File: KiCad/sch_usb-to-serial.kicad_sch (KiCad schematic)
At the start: 14 parts, among them J2 ESPFlash, Q1 MMDT3904, U3 CP2102N-Axx-xQFN24

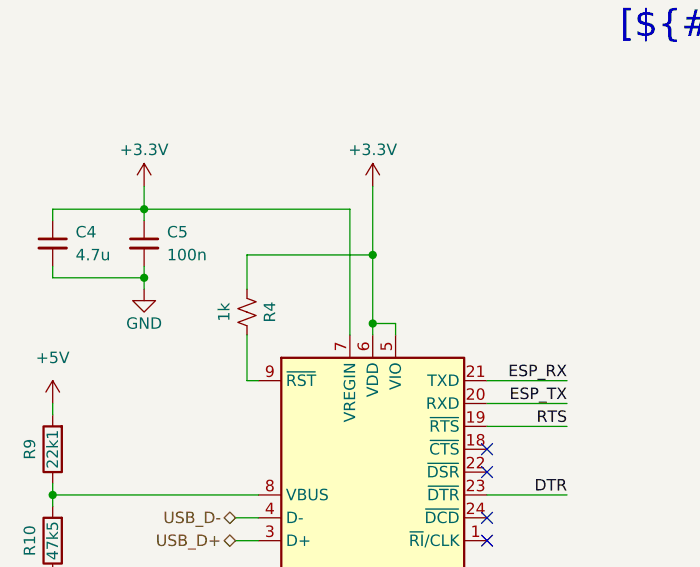
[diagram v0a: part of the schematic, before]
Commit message: Update BoM
Update components with full description and Digikey P/N.
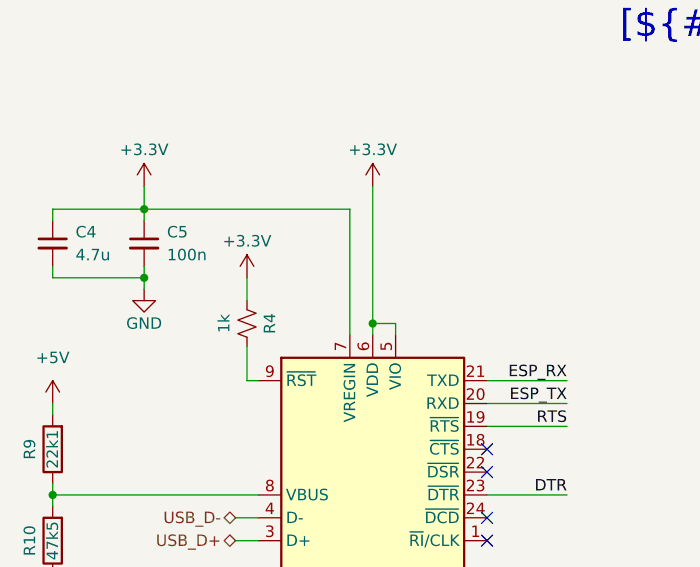
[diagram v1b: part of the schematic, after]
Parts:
- C4: footprint (none) -> Capacitor_SMD:C_0603_1608Metric; Digikey_PN (none) -> 1276-1784-1-ND
- C5: Digikey_PN (none) -> 399-C0603C104K4RACTUCT-ND
- D2: Digikey_PN (none) -> 732-4980-1-ND
- D3: Digikey_PN (none) -> 160-1434-1-ND
- J2: now left out of the parts list
- R10: Digikey_PN (none) -> 541-4050-1-ND
- R7, R8: Digikey_PN (none) -> A121523CT-ND
- R9: Digikey_PN (none) -> 541-5271-1-ND
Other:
- moved on the sheet: R4

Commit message: Update BOM and general tidy-up
Include DigiKey cut-tape components and add flag to indicate own stocked items. Remove files that aren't part of the sharable project (KiCad 9 embeds), Remove empty/irrelevant folders.
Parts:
- C5: Stocked (none) -> Yes
- R4, R6: footprint Resistor_SMD:R_0603_1608Metric_Pad0.98x0.95mm_HandSolder -> Resistor_SMD:R_0603_1608Metric; Digikey_PN 541-3993-1-ND -> MCT0603-1.00K-MFCT-ND; Stocked (none) -> Yes
- R5: footprint Resistor_SMD:R_0603_1608Metric_Pad0.98x0.95mm_HandSolder -> Resistor_SMD:R_0603_1608Metric; Digikey_PN (none) -> MCT0603-1.00K-MFCT-ND; Stocked (none) -> Yes
- R7, R8: value 10K -> 10k
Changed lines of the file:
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@@
 	(wire
 		(pts
-			(xy 215.9 50.8) (xy 228.6 50.8)
+			(xy 214.63 52.07) (xy 228.6 52.07)
 		)
 		(stroke
@@
 		(pts
 			(xy 76.2 71.12) (xy 53.34 71.12)
-		)
-		(stroke
-			(width 0)
-			(type default)
-		)
-	)
-	(wire
-		(pts
-			(xy 228.6 50.8) (xy 228.6 52.07)
 		)
 		(stroke
@@
 	(hierarchical_label "ESPFLASH_PWR"
 		(shape input)
-		(at 215.9 50.8 180)
+		(at 214.63 52.07 180)
 		(effects
 			(font
@@
 			)
 		)
-		(property "Footprint" "Resistor_SMD:R_0603_1608Metric_Pad0.98x0.95mm_HandSolder"
+		(property "Footprint" "Resistor_SMD:R_0603_1608Metric"
 			(at 151.13 48.26 0)
 			(effects
@@
 			)
 		)
-		(property "Digikey_PN" ""
+		(property "Digikey_PN" "MCT0603-1.00K-MFCT-ND"
 			(at 151.13 48.26 0)
 			(effects
@@
 					(size 1.27 1.27)
 				)
+			)
+		)
+		(property "Silk" ""
+			(at 151.13 48.26 0)
+			(effects
+				(font
+					(size 1.27 1.27)
+				)
+				(hide yes)
+			)
+		)
+		(property "Stocked" "Yes"
+			(at 151.13 48.26 0)
+			(effects
+				(font
+					(size 1.27 1.27)
+				)
+				(hide yes)
 			)
 		)
@@
 			)
 		)
-		(property "Footprint" "Resistor_SMD:R_0603_1608Metric_Pad0.98x0.95mm_HandSolder"
+		(property "Footprint" "Resistor_SMD:R_0603_1608Metric"
 			(at 74.93 52.07 0)
 			(effects
@@
 			)
 		)
-		(property "Digikey_PN" "541-3993-1-ND"
+		(property "Digikey_PN" "MCT0603-1.00K-MFCT-ND"
 			(at 74.93 52.07 0)
 			(effects
@@
 					(size 1.27 1.27)
 				)
+			)
+		)
+		(property "Silk" ""
+			(at 74.93 52.07 0)
+			(effects
+				(font
+					(size 1.27 1.27)
+				)
+				(hide yes)
+			)
+		)
+		(property "Stocked" "Yes"
+			(at 74.93 52.07 0)
+			(effects
+				(font
+					(size 1.27 1.27)
+				)
+				(hide yes)
 			)
 		)
@@
 			)
 		)
-		(property "Footprint" "Resistor_SMD:R_0603_1608Metric_Pad0.98x0.95mm_HandSolder"
+		(property "Footprint" "Resistor_SMD:R_0603_1608Metric"
 			(at 151.13 57.15 0)
 			(effects
@@
 			)
 		)
-		(property "Digikey_PN" "541-3993-1-ND"
+		(property "Digikey_PN" "MCT0603-1.00K-MFCT-ND"
 			(at 151.13 57.15 0)
 			(effects
@@
 					(size 1.27 1.27)
 				)
+				(hide yes)
+			)
+		)
+		(property "Silk" ""
+			(at 151.13 57.15 0)
+			(effects
+				(font
+					(size 1.27 1.27)
+				)
+				(hide yes)
+			)
+		)
+		(property "Stocked" "Yes"
+			(at 151.13 57.15 0)
+			(effects
+				(font
+					(size 1.27 1.27)
+				)
+				(hide yes)
 			)
 		)
@@
 			)
 		)
-		(property "Value" "10K"
+		(property "Value" "10k"
 			(at 154.94 93.98 90)
 			(effects
@@
 			)
 		)
-		(property "Value" "10K"
+		(property "Value" "10k"
 			(at 154.94 111.76 90)
 			(effects
@@
 					(size 1.27 1.27)
 				)
+			)
+		)
+		(property "Silk" ""
+			(at 154.94 111.76 0)
+			(effects
+				(font
+					(size 1.27 1.27)
+				)
+				(hide yes)
+			)
+		)
+		(property "Stocked" ""
+			(at 154.94 111.76 0)
+			(effects
+				(font
+					(size 1.27 1.27)
+				)
+				(hide yes)
 			)
 		)
@@
 			)
 		)
-		(property "Sim.Pins" ""
+		(property "Stocked" "Yes"
 			(at 63.5 43.18 0)
 			(effects
@@
 					(size 1.27 1.27)
 				)
-			)
-		)
+				(hide yes)
+			)
+		)
+		(property "Silk" ""
+			(at 63.5 43.18 0)
+			(effects
+				(font
+					(size 1.27 1.27)
+				)
+				(hide yes)
+			)
+		)

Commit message: Update project status to "Tested".
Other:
- note added: "*1"
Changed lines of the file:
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@@
+		)
+	)
+	(text "*1"
+		(exclude_from_sim no)
+		(at 157.226 37.084 0)
+		(effects
+			(font
+				(size 1.27 1.27)
+				(color 255 0 0 1)
+			)
 		)
 	)
@@
 				(thickness 0.375)
 			)
+		)
+	)
+	(text_box "* 1 - DESIGN NOTE:\n\nThe TX/RX LEDs will not light out of the box. The CP2102N UART needs to be reprogrammed using the Silicon Labs Xpress Configurator.\n\n"
+		(exclude_from_sim no)
+		(at 52.07 137.795 0)
+		(size 53.34 17.78)
+		(margins 1.2025 1.2025 1.2025 1.2025)
+		(stroke
+			(width 0.5)
+			(type solid)
+			(color 255 0 0 1)
+		)
+		(fill
+			(type none)
+		)
+		(effects
+			(font
+				(size 1.27 1.27)
+				(thickness 0.1588)
+				(color 255 0 0 1)
+			)
+			(justify left top)
+			(href "https://community.silabs.com/s/question/0D58Y00008Q3vOSSAZ/cp2102na02gqfn24-gpio0-tx-led-gpio1-rx-led-not-working?language=en_US")
 		)
 	)
@@
 			)
 		)
+		(property "Silk" ""
+			(at 53.34 76.2 0)
+			(effects
+				(font
+					(size 1.27 1.27)
+				)
+				(hide yes)
+			)
+		)
+		(property "Stocked" ""
+			(at 53.34 76.2 0)
+			(effects
+				(font
+					(size 1.27 1.27)
+				)
+				(hide yes)
+			)
+		)
